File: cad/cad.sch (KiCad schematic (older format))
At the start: 12 parts, among them J1 Input, J2 INA219 breakout, J3 Output, J4 WWG-A, J5 WWG-B, U1 L7805, U2 LM317_3PinPackage, U3 X9C103P

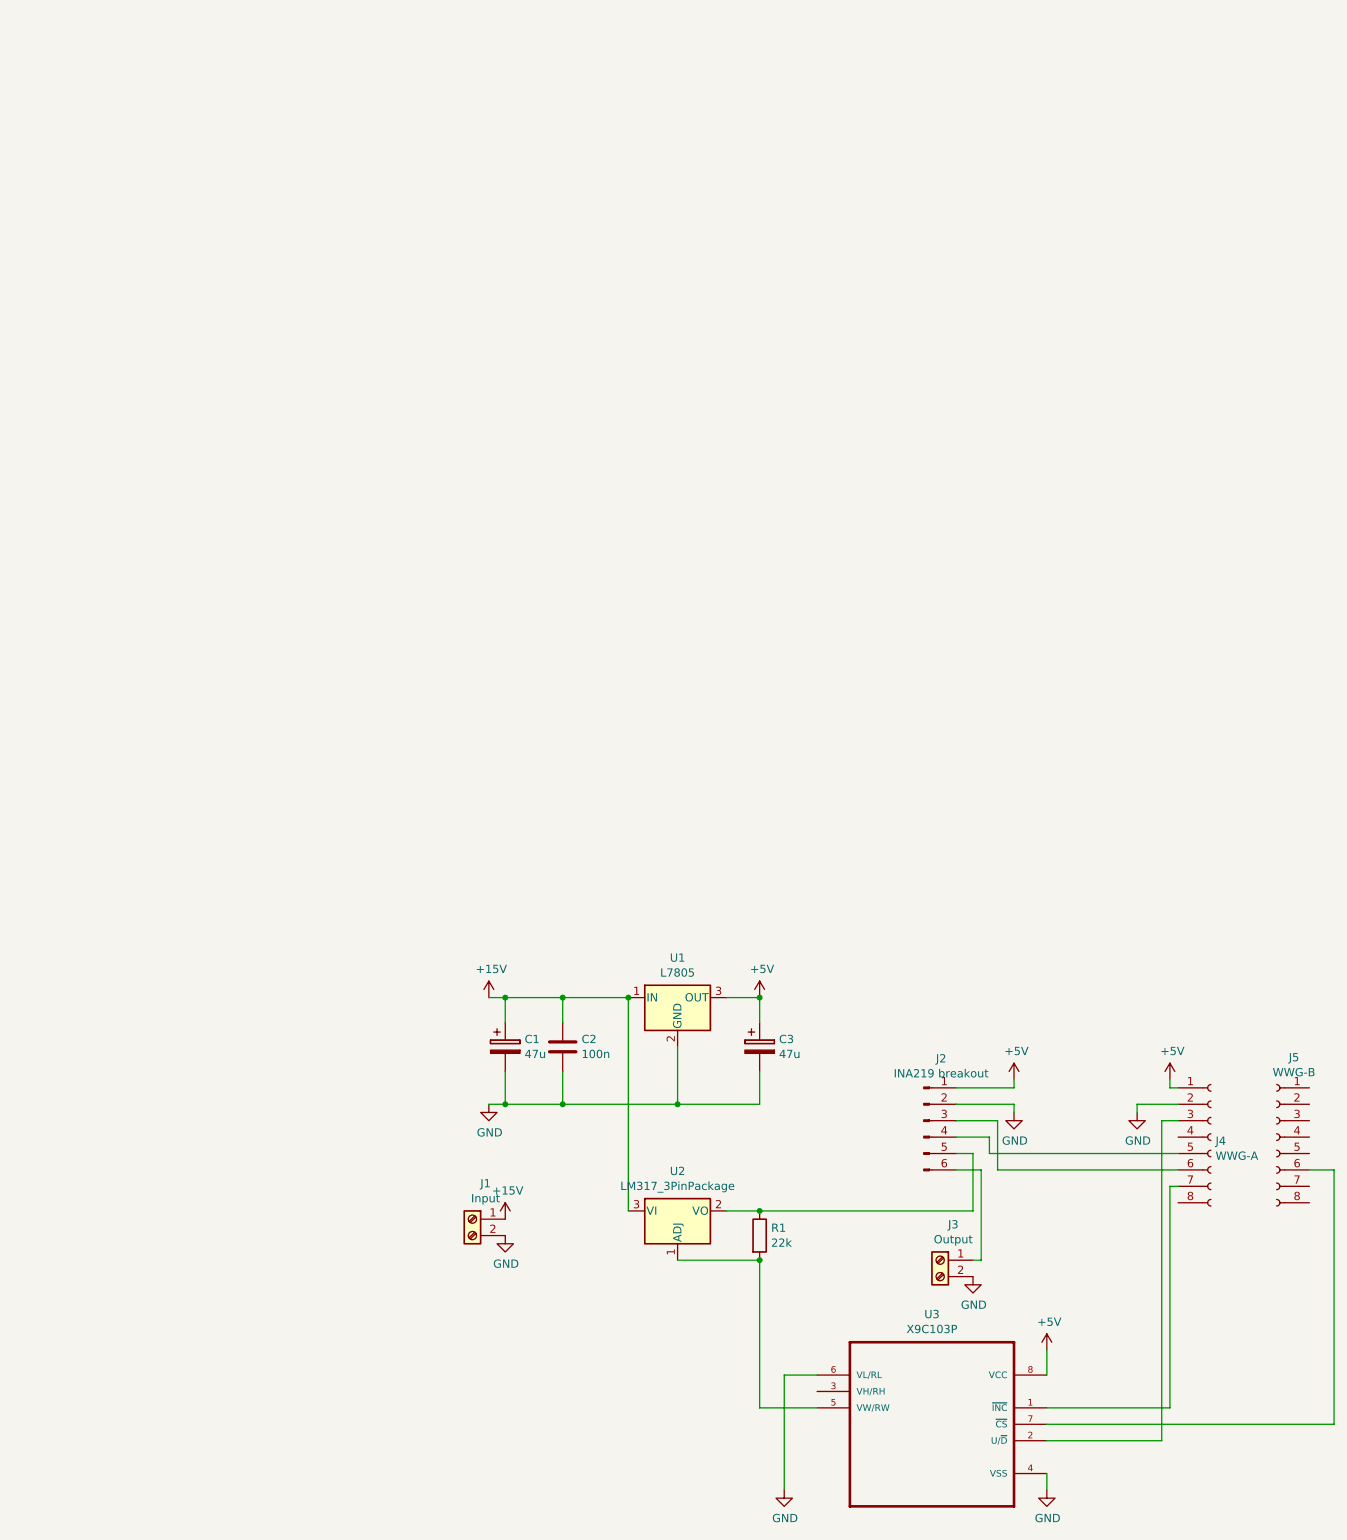
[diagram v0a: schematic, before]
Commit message: add diodes, output cap
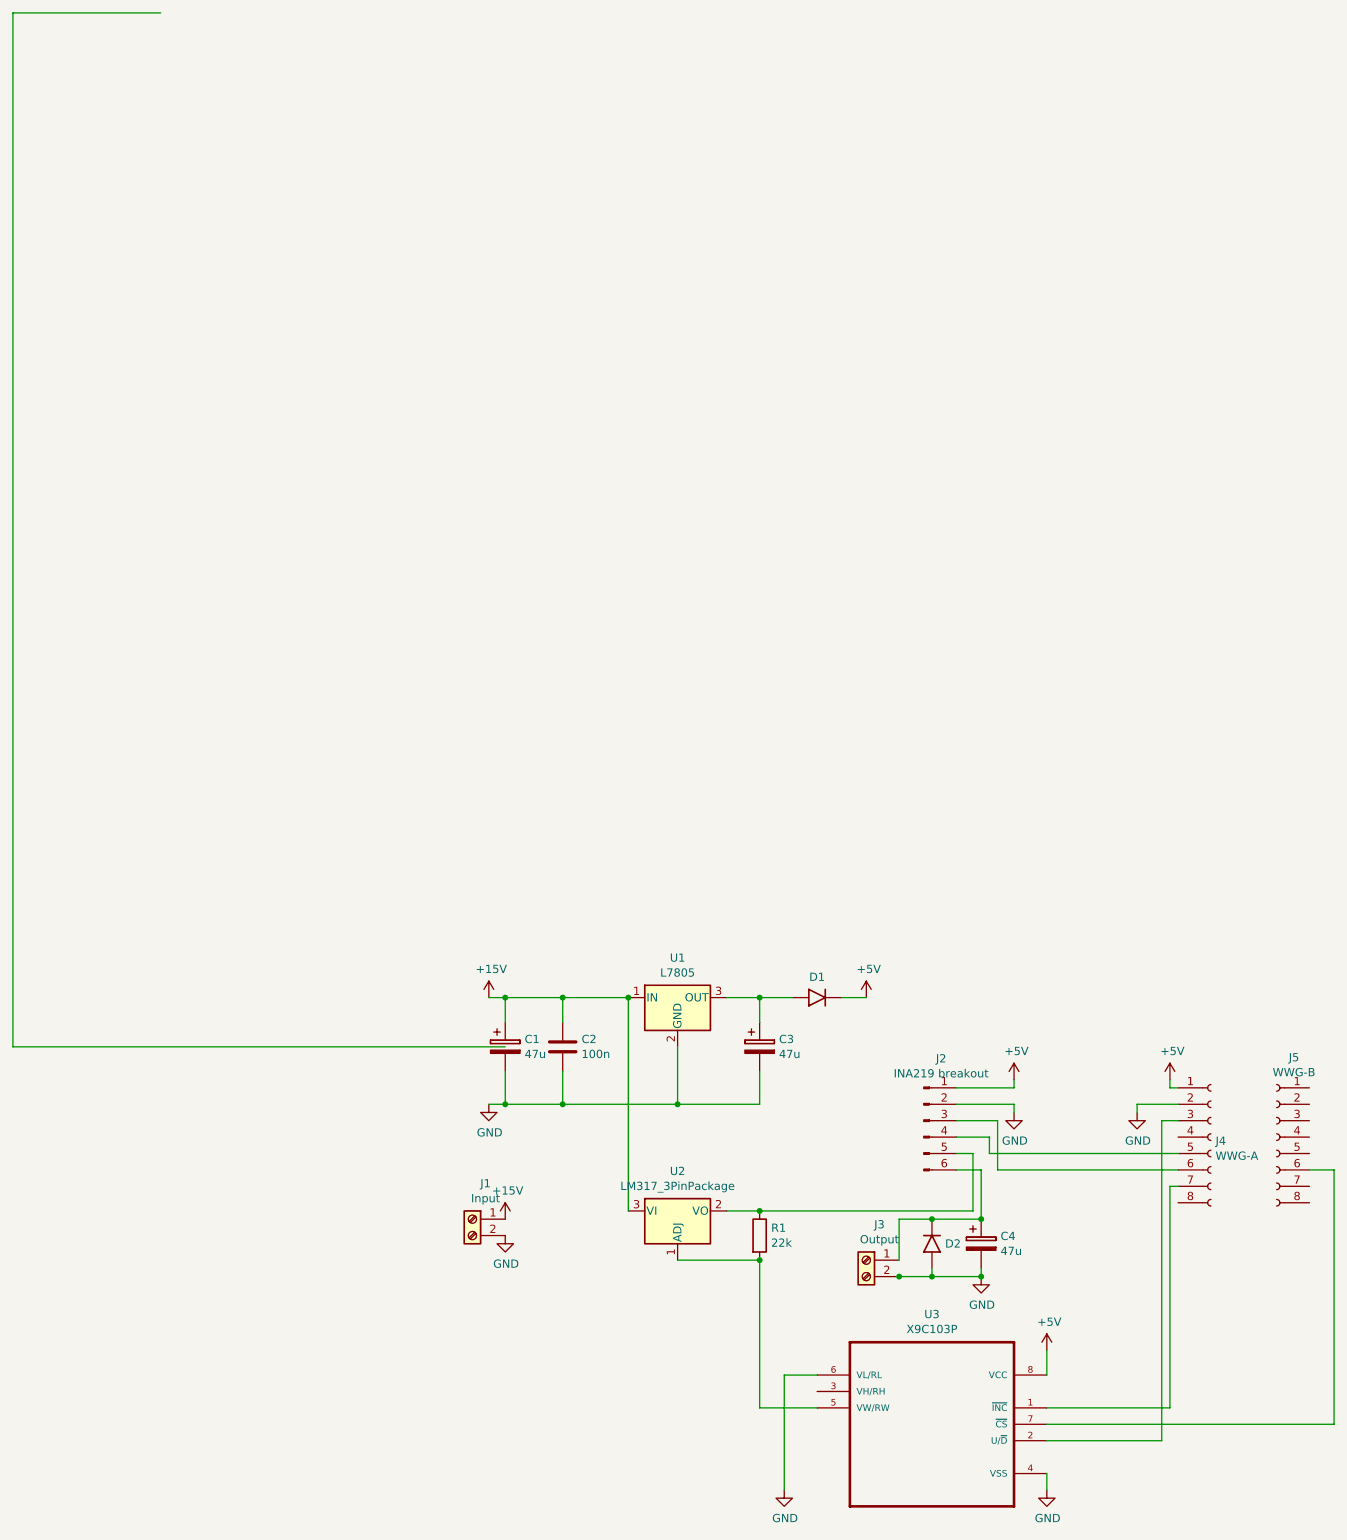
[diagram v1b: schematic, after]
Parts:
- added C4: 47u, symbol Device:CP
- added D1, D2: 1N4001, DO41-10, symbol 1N4001:1N4001
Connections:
- wire segments 53 -> 64
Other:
- moved on the sheet: J3
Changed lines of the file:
@@
 EESchema Schematic File Version 4
+LIBS:cad-cache
 EELAYER 26 0
 EELAYER END
@@
 L power:+5V #PWR0103
 U 1 1 5CD91CC6
-P 2700 1700
-F 0 "#PWR0103" H 2700 1550 50  0001 C CNN
-F 1 "+5V" H 2715 1873 50  0000 C CNN
-F 2 "" H 2700 1700 50  0001 C CNN
-F 3 "" H 2700 1700 50  0001 C CNN
-	1    2700 1700
+P 3350 1700
+F 0 "#PWR0103" H 3350 1550 50  0001 C CNN
+F 1 "+5V" H 3365 1873 50  0000 C CNN
+F 2 "" H 3350 1700 50  0001 C CNN
+F 3 "" H 3350 1700 50  0001 C CNN
+	1    3350 1700
 	1    0    0    -1
 $EndComp
@@
 L Connector:Screw_Terminal_01x02 J3
 U 1 1 5CD99328
-P 3800 3300
-F 0 "J3" H 3720 3517 50  0000 C CNN
-F 1 "Output" H 3720 3426 50  0000 C CNN
-F 2 "" H 3800 3300 50  0001 C CNN
-F 3 "~" H 3800 3300 50  0001 C CNN
-	1    3800 3300
+P 3350 3300
+F 0 "J3" H 3270 3517 50  0000 C CNN
+F 1 "Output" H 3270 3426 50  0000 C CNN
+F 2 "" H 3350 3300 50  0001 C CNN
+F 3 "~" H 3350 3300 50  0001 C CNN
+	1    3350 3300
 	-1   0    0    -1
 $EndComp
@@
 L power:GND #PWR0111
 U 1 1 5CD9960B
-P 4000 3400
-F 0 "#PWR0111" H 4000 3150 50  0001 C CNN
-F 1 "GND" H 4005 3227 50  0000 C CNN
-F 2 "" H 4000 3400 50  0001 C CNN
-F 3 "" H 4000 3400 50  0001 C CNN
-	1    4000 3400
+P 4050 3400
+F 0 "#PWR0111" H 4050 3150 50  0001 C CNN
+F 1 "GND" H 4055 3227 50  0000 C CNN
+F 2 "" H 4050 3400 50  0001 C CNN
+F 3 "" H 4050 3400 50  0001 C CNN
+	1    4050 3400
 	1    0    0    -1
 $EndComp
@@
 	3900 2750 4050 2750
 Wire Wire Line
-	4050 2750 4050 3300
-Wire Wire Line
-	4050 3300 4000 3300
+	4050 2750 4050 3050
 Wire Wire Line
 	2700 3000 4000 3000
@@
 Wire Wire Line
 	5200 2250 5250 2250
+$Comp
+L 1N4001:1N4001 D1
+U 1 1 5CE165D2
+P 3000 1700
+F 0 "D1" H 3050 1825 50  0000 C CNN
+F 1 "1N4001" H 3000 1700 50  0001 L BNN
+F 2 "DO41-10" H 3000 1700 50  0001 L BNN
+F 3 "ON Semiconductor" H 3000 1700 50  0001 L BNN
+F 4 "None" H 3000 1700 50  0001 L BNN "Field4"
+F 5 "DO-41 ON Semiconductor" H 3000 1700 50  0001 L BNN "Field5"
+F 6 "Unavailable" H 3000 1700 50  0001 L BNN "Field6"
+F 7 "1N4001" H 3000 1700 50  0001 L BNN "Field7"
+F 8 "Diode, Standard, 1A, 50V" H 3000 1700 50  0001 L BNN "Field8"
+	1    3000 1700
+	1    0    0    -1
+$EndComp
+Wire Wire Line
+	2700 1700 2900 1700
+Wire Wire Line
+	3200 1700 3350 1700
+Wire Wire Line
+	3550 3050 3550 3300
+Wire Wire Line
+	3550 3050 3750 3050
+Wire Wire Line
+	3550 3400 3750 3400
+Connection ~ 3550 3400
+Wire Wire Line
+	1150 2000 -1850 2000
+Wire Wire Line
+	-1850 2000 -1850 -4300
+Wire Wire Line
+	-1850 -4300 -950 -4300
+$Comp
+L Device:CP C4
+U 1 1 5CE1E782
+P 4050 3200
+F 0 "C4" H 4168 3246 50  0000 L CNN
+F 1 "47u" H 4168 3155 50  0000 L CNN
+F 2 "" H 4088 3050 50  0001 C CNN
+F 3 "~" H 4050 3200 50  0001 C CNN
+	1    4050 3200
+	1    0    0    -1
+$EndComp
+Connection ~ 4050 3050
+$Comp
+L 1N4001:1N4001 D2
+U 1 1 5CE1E838
+P 3750 3250
+F 0 "D2" V 3800 3170 50  0000 R CNN
+F 1 "1N4001" H 3750 3250 50  0001 L BNN
+F 2 "DO41-10" H 3750 3250 50  0001 L BNN
+F 3 "ON Semiconductor" H 3750 3250 50  0001 L BNN
+F 4 "None" H 3750 3250 50  0001 L BNN "Field4"
+F 5 "DO-41 ON Semiconductor" H 3750 3250 50  0001 L BNN "Field5"
+F 6 "Unavailable" H 3750 3250 50  0001 L BNN "Field6"
+F 7 "1N4001" H 3750 3250 50  0001 L BNN "Field7"
+F 8 "Diode, Standard, 1A, 50V" H 3750 3250 50  0001 L BNN "Field8"
+	1    3750 3250
+	0    -1   -1   0
+$EndComp
+Connection ~ 3750 3050
+Wire Wire Line
+	3750 3050 4050 3050
+Wire Wire Line
+	4050 3350 4050 3400
+Wire Wire Line
+	3750 3350 3750 3400
+Connection ~ 3750 3400
+Wire Wire Line
+	3750 3400 4050 3400
+Connection ~ 4050 3400
 $EndSCHEMATC
